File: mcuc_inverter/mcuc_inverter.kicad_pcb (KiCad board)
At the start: 4 copper layers, 200 x 132 mm, 465 parts, among them J1101 Coldplate NTC, J1201 CAN bus (H/L/GND/nc), J1202 GCT USB4085-GF-A, J1203 Aux 12-24 V in, J1204 Main contactor coil, J1205 Hall + motor temp, J1206 Encoder / SinCos, J1207 Resolver, J1208 FTSH-105-01-L-DV-K, J401 DC_INPUT_P tap - 6.3mm FASTON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, J402 to R401 chassis - 6.3mm FASTO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, J403 R401 return to DC_BUS_P tap -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, J404 from R424 chassis - 6.3mm FAS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, J405 DC_BUS_N tap - 6.3mm FASTON /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, J501 HOYS U harness - JST PA B05B-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, J502 HOYS V harness - JST PA B05B-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, J503 HOYS W harness - JST PA B05B-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, K401 HV DC precharge relay, >=450 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, Q311 BSS138 [TBV], Q321 BSS138 [TBV], Q331 BSS138 [TBV], Q341 BSS138 [TBV], Q351 BSS138 [TBV], Q361 BSS138 [TBV], Q401 AO3400-class [TBV], Q402 AO3400-class [TBV], Q403 C3M0350120J [TBV], Q601 CSD18543Q3A-class [TBV], Q602 CSD18543Q3A-class [TBV], Q603 CSD18543Q3A-class [TBV], Q604 CSD18543Q3A-class [TBV], Q605 CSD18543Q3A-class [TBV], T601 custom flyback per DER-948Q T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, T602 750316856, T603 750316856, T604 750316856, T605 750316856, U1 STM32F405VGT6, U1201 ISO1042DWR, U1202 USBLC6-2SC6, U201 FS02MR12A8MA2B, U301 1ED3491MC12M, U302 1ED3491MC12M, U303 1ED3491MC12M, U304 1ED3491MC12M, U305 1ED3491MC12M, U306 1ED3491MC12M, U401 VOM1271T, U504 TLV7032/LM2903-class open-dra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, U505 TLV7032/LM2903-class open-dra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, U506 TLV7032/LM2903-class open-dra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, U601 INN3990CQ, U603 LM5175RHFR, U604 LM74610QDGKRQ1, U605 LMR51430XDDCR, U606 LMR51430XDDCR, U607 TLV1117-33, U608 NXE2S0505MC, U609 SN6505BDBVR, U610 SN6505BDBVR, U611 SN6505BDBVR, U612 SN6505BDBVR, U701 AMC1311BDWV, U702 MCP1804T-3302I/OT, U703 TLV9061/OPA320-class [TBV], U801 AD2S1205, U802 AD8397, U803 APX809-46, U804 74LVC1G11, U901 SN74LVC00APWR, U902 SN74ALVC08PWR, U903 SN74ALVC08PWR, U904 SN74AUP1G74DCUR, Y1 8MHz, Y801 8.192MHz ABM3B [TBV]

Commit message: PCB placement complete: HV domains correct, 0 DRC violations
Resolves all 72 clearance violations that correct HV netclassification
exposed, plus the 37 from the earlier wave. The board now has 0
clearance, 0 courtyard, 0 hole and 0 parity violations with the full
HV rule set genuinely applied.

The substantive fix was structural, not cosmetic: the bus-sense
high-side block had been placed in low-voltage territory because no
pocket existed in the HV zone, and its barrier-crossing transformer
T701 - a reinforced part with 9.2 mm creepage, the element that
isolates the bus-voltage amplifier from the 450 V rail - was sitting
entirely inside LV. It now genuinely straddles: secondary pins inside
HV_DOMAIN, primary pins in LV, 11.31 mm row separation, with its own
BARRIER copper keepout on all four layers cloned from the existing
isolator barriers (17 barriers now).

The whole HV sub-block moved with it - rectifiers, reservoir and
bypass capacitors, the LDO, the divider tail - rather than being
scattered, and the LV sub-block (SN6505B driver, output stage) stayed
together below the transformer primary. No HV_DOMAIN area needed
extending; the existing polygon had room once the module's press-fit
mounting holes were routed around.

Nine of the 72 were unrelated: T601's DC_BUS_N pin against LV
decoupling. Those capacitors moved closer to the regulators they
serve as a side effect - C654 from 17 mm to 7 mm, C655 from 28 mm to
5 mm - which is better for the buck loops anyway.

One item left open honestly: C655's ground stitching via was deleted
rather than relocated, because there is no GND pour near U606 - the
module region is carved out of the plane - so the via could only
dangle. Its ground now depends on routing, like U606's other pins.

Co-Authored-By: Claude Fable 5 <noreply@anthropic.com>
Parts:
- added C1205: 4.7uF, Capacitor_SMD:C_0805_2012Metric, F.Cu at (182.4, 20.6)
- added C318: 1u 50V X7R, Capacitor_SMD:C_0805_2012Metric, F.Cu at (47.9, 105.9)
- added C319: 100n 50V X7R, Capacitor_SMD:C_0603_1608Metric, F.Cu at (42.6, 108.1)
- added C328: 1u 50V X7R, Capacitor_SMD:C_0805_2012Metric, F.Cu at (78.6, 97.9)
- added C329: 100n 50V X7R, Capacitor_SMD:C_0603_1608Metric, F.Cu at (83.1, 95.9)
- added C338: 1u 50V X7R, Capacitor_SMD:C_0805_2012Metric, F.Cu at (138.6, 106.6)
- added C339: 100n 50V X7R, Capacitor_SMD:C_0603_1608Metric, F.Cu at (142.1, 105.6)
- added C348: 1u 50V X7R, Capacitor_SMD:C_0805_2012Metric, F.Cu at (42.9, 52.4)
- added C349: 100n 50V X7R, Capacitor_SMD:C_0603_1608Metric, F.Cu at (47.4, 54.9)
- added C358: 1u 50V X7R, Capacitor_SMD:C_0805_2012Metric, F.Cu at (88.9, 55.4)
- added C359: 100n 50V X7R, Capacitor_SMD:C_0603_1608Metric, F.Cu at (86.6, 55.1)
- added C368: 1u 50V X7R, Capacitor_SMD:C_0805_2012Metric, F.Cu at (135.9, 55.4)
- added C369: 100n 50V X7R, Capacitor_SMD:C_0603_1608Metric, F.Cu at (133.6, 55.1)
- added C420: 100nF, Capacitor_SMD:C_0603_1608Metric, F.Cu at (64.4, 64.1)
- added C421: 1nF, Capacitor_SMD:C_0603_1608Metric, F.Cu at (25.6, 110.0)
- added C510: 1nF, Capacitor_SMD:C_0603_1608Metric, F.Cu at (169.9, 59.1)
- added C511: 100nF, Capacitor_SMD:C_0603_1608Metric, F.Cu at (169.9, 57.1)
- added C512: 1nF, Capacitor_SMD:C_0603_1608Metric, F.Cu at (168.6, 71.9)
- added C513: 100nF, Capacitor_SMD:C_0603_1608Metric, F.Cu at (169.9, 69.1)
- added C514: 1nF, Capacitor_SMD:C_0603_1608Metric, F.Cu at (169.9, 79.1)
- added C515: 100nF, Capacitor_SMD:C_0603_1608Metric, F.Cu at (169.9, 77.1)
- added C516: 1nF, Capacitor_SMD:C_0603_1608Metric, F.Cu at (169.9, 87.9)
- added C641: 220nF 50V X7R, Capacitor_SMD:C_0603_1608Metric, F.Cu at (104.1, 33.1)
- added C649: 220nF 50V X7R, Capacitor_SMD:C_0603_1608Metric, F.Cu at (100.0, 35.0)
- added C654: 1uF 16V X7R, Capacitor_SMD:C_0603_1608Metric, F.Cu at (94.5, 18.4)
- added C655: 1uF 16V X7R, Capacitor_SMD:C_0603_1608Metric, F.Cu at (108.0, 43.8)
- added C684: 10uF 25V X7R, Capacitor_SMD:C_0805_2012Metric, F.Cu at (42.6, 110.9)
- added C685: 10uF 25V X7R, Capacitor_SMD:C_0805_2012Metric, F.Cu at (108.1, 102.9)
- added C686: 10uF 25V X7R, Capacitor_SMD:C_0805_2012Metric, F.Cu at (144.1, 107.9)
- added C687: 10uF 25V X7R, Capacitor_SMD:C_0805_2012Metric, F.Cu at (131.9, 59.1)
- added C711: 10uF, Capacitor_SMD:C_0805_2012Metric, F.Cu at (25.5, 71.0)
- added C712: 100nF, Capacitor_SMD:C_0603_1608Metric, F.Cu at (25.5, 68.0)
- added C713: 10uF, Capacitor_SMD:C_0805_2012Metric, F.Cu at (27.2, 48.1)
- added C906: 100n, Capacitor_SMD:C_0603_1608Metric, F.Cu at (164.1, 24.1)
- added C907: 220n, Capacitor_SMD:C_0603_1608Metric, F.Cu at (165.1, 20.4)
- added D404: SMBJ24A, Diode_SMD:D_SMB, F.Cu at (33.7, 80.3)
- added D405: SMBJ24A, Diode_SMD:D_SMB, F.Cu at (8.16, 79.1)
- added D620: BZX384-C9V1 [TBV], Diode_SMD:D_SOD-323, F.Cu at (42.0, 42.6)
- added D621: MMSZ5245C-E3-08 15V 2%, Diode_SMD:D_SOD-123, F.Cu at (47.0, 109.1)
- added D622: MMSZ5245C-E3-08 15V 2%, Diode_SMD:D_SOD-123, F.Cu at (87.5, 96.8)
- added D623: MMSZ5245C-E3-08 15V 2%, Diode_SMD:D_SOD-123, F.Cu at (138.8, 110.6)
- added D624: MMSZ5245C-E3-08 15V 2%, Diode_SMD:D_SOD-123, F.Cu at (128.0, 59.6)
- added D625: 1N4148W-7-F, Diode_SMD:D_SOD-123, F.Cu at (51.1, 109.5)
- added D626: 1N4148W-7-F, Diode_SMD:D_SOD-123, F.Cu at (103.5, 103.6)
- added D627: 1N4148W-7-F, Diode_SMD:D_SOD-123, F.Cu at (144.0, 110.6)
- added D628: 1N4148W-7-F, Diode_SMD:D_SOD-123, F.Cu at (124.1, 59.5)
- added D629: SMCJ36CA, Diode_SMD:D_SMC, F.Cu at (82.0, 51.1)
- added D630: MMSZ5243BT1G 13V, Diode_SMD:D_SOD-123, F.Cu at (94.8, 14.3)
- added D701: SS310 [TBV], Diode_SMD:D_SMC, F.Cu at (33.5, 43.4)
- added D702: SS310 [TBV], Diode_SMD:D_SMC, F.Cu at (23.0, 43.4)
- added D904: BAT54WS, Diode_SMD:D_SOD-323, F.Cu at (162.1, 24.0)
- added J406: PHASE_U motor output stud - M6 ring lug [TBV], MountingHole:MountingHole_6.4mm_M6_Pad_Via, F.Cu at (148.6, 124.1)
- added J407: PHASE_V motor output stud - M6 ring lug [TBV], MountingHole:MountingHole_6.4mm_M6_Pad_Via, F.Cu at (167.1, 124.1)
- added J408: PHASE_W motor output stud - M6 ring lug [TBV], MountingHole:MountingHole_6.4mm_M6_Pad_Via, F.Cu at (178.6, 105.1)
- added JP1201: TERM_H, Jumper:SolderJumper-2_P1.3mm_Bridged_RoundedPad1.0x1.5mm, F.Cu at (182.7, 24.3)
- added JP1202: TERM_L, Jumper:SolderJumper-2_P1.3mm_Bridged_RoundedPad1.0x1.5mm, F.Cu at (167.4, 24.1)
- added Q404: BSS138, Package_TO_SOT_SMD:SOT-23, F.Cu at (21.6, 110.0)
- added Q606: BCP56-16T1G, Package_TO_SOT_SMD:SOT-223-3_TabPin2, F.Cu at (57.8, 107.3)
- added Q607: BCP56-16T1G, Package_TO_SOT_SMD:SOT-223-3_TabPin2, F.Cu at (115.6, 100.3)
- added Q608: BCP56-16T1G, Package_TO_SOT_SMD:SOT-223-3_TabPin2, F.Cu at (151.8, 107.3)
- added Q609: BCP56-16T1G, Package_TO_SOT_SMD:SOT-223-3_TabPin2, F.Cu at (118.3, 57.6)
- added Q610: DMP6023LE-13, Package_TO_SOT_SMD:SOT-223-3_TabPin2, F.Cu at (139.3, 64.3)
- added R317: 2.49k 1% (zener preload 6.0mA), Resistor_SMD:R_1206_3216Metric, F.Cu at (41.3, 104.7)
- added R327: 2.49k 1% (zener preload 6.0mA), Resistor_SMD:R_1206_3216Metric, F.Cu at (82.4, 98.3)
- added R337: 2.49k 1% (zener preload 6.0mA), Resistor_SMD:R_1206_3216Metric, F.Cu at (135.3, 104.7)
- added R347: 2.49k 1% (zener preload 6.0mA), Resistor_SMD:R_1206_3216Metric, F.Cu at (43.9, 55.0)
- added R428: 10k, Resistor_SMD:R_0603_1608Metric, F.Cu at (27.0, 107.2)
- added R429: 10k, Resistor_SMD:R_0603_1608Metric, F.Cu at (66.4, 64.1)
- added R513: 100R, Resistor_SMD:R_0603_1608Metric, F.Cu at (172.6, 58.4)
- added R514: 100k, Resistor_SMD:R_0603_1608Metric, F.Cu at (167.1, 58.4)
- added R515: 1M, Resistor_SMD:R_0603_1608Metric, F.Cu at (168.6, 61.9)
- added R517: 100R, Resistor_SMD:R_0603_1608Metric, F.Cu at (169.9, 67.1)
- added R518: 100k, Resistor_SMD:R_0603_1608Metric, F.Cu at (169.9, 65.1)
- added R519: 1M, Resistor_SMD:R_0603_1608Metric, F.Cu at (167.1, 68.4)
- added R521: 100R, Resistor_SMD:R_0603_1608Metric, F.Cu at (167.1, 79.9)
- added R522: 100k, Resistor_SMD:R_0603_1608Metric, F.Cu at (165.1, 79.9)
- added R523: 1M, Resistor_SMD:R_0603_1608Metric, F.Cu at (170.9, 84.9)
- added R612: 39k, Resistor_SMD:R_1206_3216Metric, F.Cu at (30.3, 4.20)
- added R613: 39k, Resistor_SMD:R_1206_3216Metric, F.Cu at (27.5, 4.45)
- added R614: 39k, Resistor_SMD:R_1206_3216Metric, F.Cu at (24.8, 4.45)
- added R615: 39k, Resistor_SMD:R_1206_3216Metric, F.Cu at (22.0, 4.45)
- added R616: 300k, Resistor_SMD:R_1206_3216Metric, F.Cu at (43.3, 3.69)
- added R617: 300k, Resistor_SMD:R_1206_3216Metric, F.Cu at (41.5, 29.0)
- added R618: 300k, Resistor_SMD:R_1206_3216Metric, F.Cu at (41.5, 34.0)
- added R619: 300k, Resistor_SMD:R_1206_3216Metric, F.Cu at (41.5, 39.0)
- added R630: 210k, Resistor_SMD:R_0603_1608Metric, F.Cu at (42.0, 45.3)
- added R644: 470R 1%, Resistor_SMD:R_0603_1608Metric, F.Cu at (39.6, 110.4)
- added R645: 470R 1%, Resistor_SMD:R_0603_1608Metric, F.Cu at (105.4, 95.9)
- added R646: 470R 1%, Resistor_SMD:R_0603_1608Metric, F.Cu at (134.4, 111.1)
- added R647: 470R 1%, Resistor_SMD:R_0603_1608Metric, F.Cu at (127.1, 57.1)
- added R648: 100k, Resistor_SMD:R_0603_1608Metric, F.Cu at (93.9, 9.89)
- added R840: 1.00k, Resistor_SMD:R_0603_1608Metric, F.Cu at (185.9, 23.1)
- added R841: 10.0k, Resistor_SMD:R_0603_1608Metric, F.Cu at (189.4, 23.1)
- added T701: 750313734, mcuc:WE_750313734, F.Cu at (20.3, 57.5)
- added U402: SN74LVC1G97DBVR, Package_TO_SOT_SMD:SOT-23-6, F.Cu at (36.4, 62.7)
- added U507: OPA376AIDBVR, Package_TO_SOT_SMD:SOT-23-5, F.Cu at (172.0, 62.1)
- added U508: OPA376AIDBVR, Package_TO_SOT_SMD:SOT-23-5, F.Cu at (172.0, 72.1)
- added U509: OPA376AIDBVR, Package_TO_SOT_SMD:SOT-23-5, F.Cu at (172.0, 82.1)
- added U704: SN6505BDBVR, Package_TO_SOT_SMD:SOT-23-6, F.Cu at (20.5, 67.5)
- C1, C1101, C1102, C12, C1201, C1202, C1203, C13, C14, C2, C3, C311, C312, C314, C316, C321, C322, C324, C326, C331, C332, C334, C336, C341, C342, C344, C346, C351, C352, C354, C356, C361, C362, C364, C366, C4, C5, C501, C502, C503, C504, C505, C506, C507, C508, C509, C6, C611, C613, C622, C623, C624, C625, C626, C627, C631, C642, C646, C652, C661, C663, C665, C667, C669, C671, C673, C675, C677, C679, C681, C683, C701, C702, C706, C707, C708, C709, C710, C8, C801, C802, C803, C804, C805, C806, C807, C808, C809, C810, C811, C812, C813, C814, C815, C817, C819, C820, C9, C901, C902, C903, C904, C905: footprint C_0603_1608Metric -> Capacitor_SMD:C_0603_1608Metric
- C10, C11, C1204, C313, C315, C323, C325, C333, C335, C343, C345, C353, C355, C363, C365, C620, C621, C650, C651, C653, C660, C662, C664, C666, C668, C670, C672, C674, C676, C678, C680, C682, C7: footprint C_0805_2012Metric -> Capacitor_SMD:C_0805_2012Metric
- C317, C327, C337, C347, C357, C367: value 100p [TBV] -> 22p 50V C0G - DNP; footprint C_0603_1608Metric -> Capacitor_SMD:C_0603_1608Metric
- C601, C602: value 0.68uF 630V film [TBV] -> 0.68uF 630VDC X2 film; footprint C_0603_1608Metric -> Capacitor_THT:C_Rect_L26.5mm_W10.5mm_P22.50mm_MKS4
- C603: value 10nF 1kV [TBV] -> 6.8nF 630V C0G; footprint C_0603_1608Metric -> Capacitor_SMD:C_1210_3225Metric
- C604: value 10uF 50V [TBV] -> 10uF 50V X7R; footprint C_0603_1608Metric -> Capacitor_SMD:C_1210_3225Metric
- C606: value 4.7uF 25V X7R [TBV] -> 0.47uF 50V X7R; footprint C_0603_1608Metric -> Capacitor_SMD:C_0805_2012Metric
- C607: value 100nF [TBV] -> 100nF 50V X7R; footprint C_0603_1608Metric -> Capacitor_SMD:C_0805_2012Metric
- C608: value 1nF 100V [TBV] -> 1nF 200V C0G; footprint C_0603_1608Metric -> Capacitor_SMD:C_0805_2012Metric
- C609, C610: footprint CP_Elec_8x10.5 -> Capacitor_SMD:CP_Elec_8x10.5
- C612: value 330pF [TBV] -> 270pF; footprint C_0603_1608Metric -> Capacitor_SMD:C_0603_1608Metric
- C614: footprint C_0603_1608Metric -> Capacitor_SMD:C_0805_2012Metric
- C628: value 100pF [TBV] -> 130pF; footprint C_0603_1608Metric -> Capacitor_SMD:C_0603_1608Metric
- C629, C630, C643, C644, C647, C648: footprint C_1210_3225Metric -> Capacitor_SMD:C_1210_3225Metric
- C640, C645: value 2.2uF 50V [TBV] -> 10uF 50V X7R; footprint C_0805_2012Metric -> Capacitor_SMD:C_1210_3225Metric
- C703: value 100nF -> 100pF; footprint C_0603_1608Metric -> Capacitor_SMD:C_0603_1608Metric
- C816, C818: value 100nF -> 1nF; footprint C_0603_1608Metric -> Capacitor_SMD:C_0603_1608Metric
- D1201, D801, D802, D803, D804, D805, D806, D807, D808, D809, D901, U803: footprint SOT-23 -> Package_TO_SOT_SMD:SOT-23
- D1202, D1203: footprint LED_0805_2012Metric -> LED_SMD:LED_0805_2012Metric
- D311, D321, D331, D341, D351, D361, D602: footprint D_SOD-323 -> Diode_SMD:D_SOD-323
- D312, D313, D322, D323, D332, D333, D342, D343, D352, D353, D362, D363, D601: footprint D_SMA -> Diode_SMD:D_SMA
- D401: value BAS316 [TBV] -> ES1G; footprint D_SOD-323 -> Diode_SMD:D_SMA
- D402: value BAS316 [TBV] -> ES2G; footprint D_SOD-323 -> Diode_SMD:D_SMB
- D403: value MM3Z18VT1G -> MMSZ5245BT1G; footprint D_SOD-323 -> Diode_SMD:D_SOD-123
- D603, D604, D605, D606, D608, D609, D611, D612, D614, D615: footprint D_SMC -> Diode_SMD:D_SMC
- D607, D610, D613, D616: value BZX384-C5V1 [TBV] -> MM3Z4V7ST1G 4.7V; footprint D_SOD-323 -> Diode_SMD:D_SOD-323
- D902: value OCP -> APT2012SURCK red (OCP); footprint LED_0805_2012Metric -> LED_SMD:LED_0805_2012Metric
- D903: value FAULT -> APT2012SYCK amber (DRV FLT); footprint LED_0805_2012Metric -> LED_SMD:LED_0805_2012Metric
- E801, FB1: footprint L_0805_2012Metric -> Inductor_SMD:L_0805_2012Metric
- J1101: footprint JST_PH_B2B-PH-K_1x02_P2.00mm_Vertical -> Connector_JST:JST_PH_B2B-PH-K_1x02_P2.00mm_Vertical
- J1201: footprint JST_PH_B4B-PH-K_1x04_P2.00mm_Vertical -> Connector_JST:JST_PH_B4B-PH-K_1x04_P2.00mm_Vertical
- J1202: footprint USB_C_Receptacle_GCT_USB4085 -> Connector_USB:USB_C_Receptacle_GCT_USB4085
- J1203: footprint JST_VH_B2P-VH_1x02_P3.96mm_Vertical -> Connector_JST:JST_VH_B2P-VH_1x02_P3.96mm_Vertical
- J1204: footprint JST_VH_B4P-VH_1x04_P3.96mm_Vertical -> Connector_JST:JST_VH_B4P-VH_1x04_P3.96mm_Vertical
- J1205, J1206: footprint JST_SH_SM08B-SRSS-TB_1x08-1MP_P1.00mm_Horizontal -> Connector_JST:JST_SH_SM08B-SRSS-TB_1x08-1MP_P1.00mm_Horizontal
- J1207: footprint JST_SH_SM06B-SRSS-TB_1x06-1MP_P1.00mm_Horizontal -> Connector_JST:JST_SH_SM06B-SRSS-TB_1x06-1MP_P1.00mm_Horizontal
- J1208: footprint PinHeader_2x05_P1.27mm_Vertical_SMD -> Connector_PinHeader_1.27mm:PinHeader_2x05_P1.27mm_Vertical_SMD
- J401, J402, J403, J404, J405: footprint MountingHole_4.3mm_M4_Pad_Via -> MountingHole:MountingHole_4.3mm_M4_Pad_Via
- J501, J502, J503: footprint JST_PH_B5B-PH-K_1x05_P2.00mm_Vertical -> mcuc:JST_PA_B05B-PASK-1_1x05_P2.00mm_Vertical
- K401: value HV DC precharge relay, >=450 V DC contacts [TBV] -> HFE80V-20C/450-12-HTPAJ; footprint HFE80V_HTPAJ -> mcuc:HFE80V_HTPAJ
- L601: footprint L_Bourns_SRP6060FA -> Inductor_SMD:L_Bourns_SRP6060FA
- L602: value SRP5030TA-4R7M 4.7uH 6A -> SRP6060FA-100M 10uH 7.6A; footprint L_Bourns_SRP5030T -> Inductor_SMD:L_Bourns_SRP6060FA
- L603: footprint L_Bourns_SRR1260 -> Inductor_SMD:L_Bourns_SRR1260
- Q311, Q321, Q331, Q341, Q351, Q361: value BSS138 [TBV] -> BSS316N; footprint SOT-23 -> Package_TO_SOT_SMD:SOT-23
- Q401: value AO3400-class [TBV] -> NVR5198NLT1G; footprint SOT-23 -> Package_TO_SOT_SMD:SOT-23
- Q402: value AO3400-class [TBV] -> DMN6068LK3-13; footprint SOT-23 -> Package_TO_SOT_SMD:TO-252-3_TabPin2
- Q403: footprint TO-263-7_TabPin8 -> Package_TO_SOT_SMD:TO-263-7_TabPin8
- Q601, Q602, Q603, Q604, Q605: footprint VSON-8_3.3x3.3mm_P0.65mm_NexFET -> Package_SON:VSON-8_3.3x3.3mm_P0.65mm_NexFET
- R1, R1101, R1102, R1103, R1104, R1202, R1203, R1204, R1205, R1206, R1207, R1208, R1209, R311, R321, R331, R341, R351, R361, R391, R392, R393, R402, R403, R404, R405, R425, R426, R501, R505, R509, R606, R607, R609, R610, R611, R620, R621, R624, R625, R626, R627, R705, R706, R707, R708, R801, R802, R803, R804, R805, R806, R807, R808, R809, R810, R811, R812, R813, R814, R815, R821, R822, R823, R824, R825, R826, R827, R828, R829, R830, R831, R832, R833, R836, R839, R901, R902, R903, R904, R905, R906, R907, R908, R909, R910, R913, R914, RT1101: footprint R_0603_1608Metric -> Resistor_SMD:R_0603_1608Metric
- R312, R322, R332, R342, R352, R362: value 4.87k [TBV] -> 28.0k 1% (ADJA: soft-off 699mA); footprint R_0603_1608Metric -> Resistor_SMD:R_0603_1608Metric
- R313, R323, R333, R343, R353, R363: value 1.33k [TBV] -> 0R link (ADJB=VCC1); footprint R_0603_1608Metric -> Resistor_SMD:R_0603_1608Metric
- R314, R324, R334, R344, R354, R364: value 12 [TBV] -> 12R 1% 0.75W CRCW1206-HP; footprint R_1206_3216Metric -> Resistor_SMD:R_1206_3216Metric
- R315, R325, R335, R345, R355, R365: value 3.3 [TBV] -> 3R3 1% 0.75W CRCW1206-HP; footprint R_1206_3216Metric -> Resistor_SMD:R_1206_3216Metric
- R316, R326, R336, R346, R356, R366, R701, R702, R703, R704: footprint R_1206_3216Metric -> Resistor_SMD:R_1206_3216Metric
- R411, R412, R413, R414: value 18.7k 3W [TBV] -> 14k 2W; footprint R_2512_6332Metric -> Resistor_SMD:R_2512_6332Metric
- R427: value 100R -> 220R; footprint R_0603_1608Metric -> Resistor_SMD:R_0603_1608Metric
- R502, R506, R510: value 9.53k -> 6.19k 0.1%; footprint R_0603_1608Metric -> Resistor_SMD:R_0603_1608Metric
- R503, R507, R511: value 13.7k -> 6.19k 0.1%; footprint R_0603_1608Metric -> Resistor_SMD:R_0603_1608Metric
- R504, R508, R512: value 9.53k -> 8.62k 0.1%; footprint R_0603_1608Metric -> Resistor_SMD:R_0603_1608Metric
- R603, R604: value 390k 0.5W [TBV] -> 39k; footprint R_0603_1608Metric -> Resistor_SMD:R_1206_3216Metric
- R605: value 4.7R 0.5W [TBV] -> 4.7R; footprint R_0603_1608Metric -> Resistor_SMD:R_1206_3216Metric
- R608: value 10R [TBV] -> 10R; footprint R_0603_1608Metric -> Resistor_SMD:R_1206_3216Metric
- R622: value 10mR 1% [TBV] -> 30mR 1%; footprint R_2512_6332Metric -> Resistor_SMD:R_2512_6332Metric
- R623: value 88.7k 1% -> 97.6k 1%; footprint R_0603_1608Metric -> Resistor_SMD:R_0603_1608Metric
- R640: value 71.5k 1% -> 100k 1%; footprint R_0603_1608Metric -> Resistor_SMD:R_0603_1608Metric
- R641: value 9.76k 1% -> 24.9k 1%; footprint R_0603_1608Metric -> Resistor_SMD:R_0603_1608Metric
- R642: value 115k 1% -> 100k 1%; footprint R_0603_1608Metric -> Resistor_SMD:R_0603_1608Metric
- R643: value 6.04k 1% -> 9.09k 1%; footprint R_0603_1608Metric -> Resistor_SMD:R_0603_1608Metric
- R709, R710: value 7.50k -> 15.0k; footprint R_0603_1608Metric -> Resistor_SMD:R_0603_1608Metric
- R816, R817, R818: value 0R -> 1k; footprint R_0603_1608Metric -> Resistor_SMD:R_0603_1608Metric
- R834, R837: value 100k -> 10k; footprint R_0603_1608Metric -> Resistor_SMD:R_0603_1608Metric
- R835, R838: value 270k -> 27k; footprint R_0603_1608Metric -> Resistor_SMD:R_0603_1608Metric
- R911, R912: value 100R -> 2.2k; footprint R_0603_1608Metric -> Resistor_SMD:R_0603_1608Metric
- T601: footprint T_FLYBACK_EQ30 -> mcuc:T_FLYBACK_EQ30
- T602, T603, T604, T605: footprint WE_PPTI_750316856 -> mcuc:WE_PPTI_750316856
- TP1101, TP1102, TP1103, TP1104, TP1105, TP1106: footprint TestPoint_Pad_D1.5mm -> TestPoint:TestPoint_Pad_D1.5mm
- U1: footprint LQFP-100_14x14mm_P0.5mm -> Package_QFP:LQFP-100_14x14mm_P0.5mm
- U1201: footprint SOIC-16W_7.5x10.3mm_P1.27mm -> Package_SO:SOIC-16W_7.5x10.3mm_P1.27mm
- U1202, U609, U610, U611, U612: footprint SOT-23-6 -> Package_TO_SOT_SMD:SOT-23-6
- U201: footprint FS02MR12A8MA2B_PressFIT -> mcuc:FS02MR12A8MA2B_PressFIT
- U301, U302, U303, U304, U305, U306: footprint PG-DSO-16-28 -> mcuc:PG-DSO-16-28
- U401: footprint SOP-4_3.8x4.1mm_P2.54mm -> Package_SO:SOP-4_3.8x4.1mm_P2.54mm
- U504, U505, U506: value TLV7032/LM2903-class open-drain [TBV] -> TLV7022DDFR; footprint SOIC-8_3.9x4.9mm_P1.27mm -> Package_TO_SOT_SMD:Texas_DDF0008A_SOT-8_1.6x2.9mm_P0.65mm
- U601: footprint InSOP-24D -> mcuc:InSOP-24D
- U603: footprint VQFN-28-1EP_4x5mm_P0.5mm_EP2.55x3.55mm -> Package_DFN_QFN:VQFN-28-1EP_4x5mm_P0.5mm_EP2.55x3.55mm
- U604: footprint VSSOP-8_3x3mm_P0.65mm -> Package_SO:VSSOP-8_3x3mm_P0.65mm
- U605, U606: value LMR51430XDDCR -> LMR33630ADDAR; footprint SOT-23-6 -> Package_SO:SOIC-8-1EP_3.9x4.9mm_P1.27mm_EP2.95x4.9mm_Mask2.71x3.4mm
- U607: footprint SOT-223-3_TabPin2 -> Package_TO_SOT_SMD:SOT-223-3_TabPin2
- U608: footprint Converter_DCDC_Murata_NXExSxxxxMC_SMD -> Converter_DCDC:Converter_DCDC_Murata_NXExSxxxxMC_SMD
- U701: footprint SOIC-8_7.5x5.85mm_P1.27mm -> Package_SO:SOIC-8_7.5x5.85mm_P1.27mm
- U702, U703: footprint SOT-23-5 -> Package_TO_SOT_SMD:SOT-23-5
- U801: footprint LQFP-44_10x10mm_P0.8mm -> Package_QFP:LQFP-44_10x10mm_P0.8mm
- U802: footprint SOIC-8-1EP_3.9x4.9mm_P1.27mm_EP2.29x3mm -> Package_SO:SOIC-8-1EP_3.9x4.9mm_P1.27mm_EP2.29x3mm
- U804: footprint SOT-363_SC-70-6 -> Package_TO_SOT_SMD:SOT-363_SC-70-6
- U901, U902, U903: footprint TSSOP-14_4.4x5mm_P0.65mm -> Package_SO:TSSOP-14_4.4x5mm_P0.65mm
- U904: footprint VSSOP-8_2.3x2mm_P0.5mm -> Package_SO:VSSOP-8_2.3x2mm_P0.5mm
- Y1: footprint Crystal_SMD_5032-2Pin_5.0x3.2mm -> Crystal:Crystal_SMD_5032-2Pin_5.0x3.2mm
- Y801: footprint Crystal_SMD_Abracon_ABM3B-4Pin_5.0x3.2mm -> Crystal:Crystal_SMD_Abracon_ABM3B-4Pin_5.0x3.2mm
- moved C602 112.2 mm to (90.9, 125.7)
- moved C601 104.2 mm to (90.9, 113.9)
- moved L602 63.5 mm to (83.5, 76.6), turned to 90 degrees
- moved R707 35.3 mm to (62.1, 61.4)
- moved R405 34.7 mm to (62.4, 64.1), turned to 90 degrees
- moved R403 33.4 mm to (1.90, 90.9), turned to 90 degrees
- moved R402 28.2 mm to (58.6, 61.9)
- moved D402 25.0 mm to (3.16, 79.1), turned to 90 degrees
- moved U606 22.4 mm to (117.1, 42.9), turned to 0 degrees
- moved R708 20.4 mm to (3.89, 61.9)
- moved C346 20.0 mm to (51.6, 61.4), turned to 0 degrees
- moved U605 19.1 mm to (100.1, 14.6), turned to 0 degrees
- moved D401 18.4 mm to (18.9, 79.5)
- moved R710 18.0 mm to (37.1, 78.1)
- moved R404 16.9 mm to (1.90, 63.1)
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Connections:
- net Net-(D403-K) renamed /Precharge and contactor/Q403_G
- C602 pad 2: /Auxiliary power/DC_BUS_N -> /Precharge and contactor/DC_BUS_N
- C603 pad 2: Net-(C603-Pad2) -> /Auxiliary power/CLAMP_NODE
- C604 pad 2: /Auxiliary power/DC_BUS_N -> /Precharge and contactor/DC_BUS_N
- C606 pad 2: /Auxiliary power/DC_BUS_N -> /Precharge and contactor/DC_BUS_N
- C607 pad 2: /Auxiliary power/DC_BUS_N -> /Precharge and contactor/DC_BUS_N
- C620 pad 1: /AUX_IN -> /Auxiliary power/AUX_IN_P
- C621 pad 1: /AUX_IN -> /Auxiliary power/AUX_IN_P
- C642 pad 1: Net-(U605-CB) -> Net-(U605-BOOT)
- C646 pad 1: Net-(U606-CB) -> Net-(U606-BOOT)
- C662 pad 1: /VGD_HS1_P -> /Auxiliary power/VGD_HS1_RAW
- C663 pad 1: /VGD_HS1_P -> /Auxiliary power/VGD_HS1_RAW
- C668 pad 1: /VGD_HS2_P -> /Auxiliary power/VGD_HS2_RAW
- C669 pad 1: /VGD_HS2_P -> /Auxiliary power/VGD_HS2_RAW
- C674 pad 1: /VGD_HS3_P -> /Auxiliary power/VGD_HS3_RAW
- C675 pad 1: /VGD_HS3_P -> /Auxiliary power/VGD_HS3_RAW
- C680 pad 1: /VGD_LS_P -> /Auxiliary power/VGD_LS_RAW
- C681 pad 1: /VGD_LS_P -> /Auxiliary power/VGD_LS_RAW
- C701 pad 1: /VGD_LS_P -> /Bus voltage sensing/5V5_HV_RAW
- C701 pad 2: /VGD_LS_COM -> /Precharge and contactor/DC_BUS_N
- C702 pad 1: unconnected-(C702-Pad1) -> /Bus voltage sensing/3V3_HV
- C702 pad 2: /VGD_LS_COM -> /Precharge and contactor/DC_BUS_N
- C703 pad 2: /Auxiliary power/DC_BUS_N -> /Precharge and contactor/DC_BUS_N
- C706 pad 2: /Auxiliary power/DC_BUS_N -> /Precharge and contactor/DC_BUS_N
- C707 pad 2: /Auxiliary power/DC_BUS_N -> /Precharge and contactor/DC_BUS_N
- D401 pad 1: +12V -> Net-(D401-K)
- D402 pad 1: +12V -> Net-(D402-K)
- D403 pad 2: /Auxiliary power/DC_BUS_N -> /Precharge and contactor/DC_BUS_N
- D605 pad 1: /VGD_HS1_P -> /Auxiliary power/VGD_HS1_RAW
- D606 pad 1: /VGD_HS1_P -> /Auxiliary power/VGD_HS1_RAW
- D608 pad 1: /VGD_HS2_P -> /Auxiliary power/VGD_HS2_RAW
- D609 pad 1: /VGD_HS2_P -> /Auxiliary power/VGD_HS2_RAW
- D611 pad 1: /VGD_HS3_P -> /Auxiliary power/VGD_HS3_RAW
- D612 pad 1: /VGD_HS3_P -> /Auxiliary power/VGD_HS3_RAW
- D614 pad 1: /VGD_LS_P -> /Auxiliary power/VGD_LS_RAW
- D615 pad 1: /VGD_LS_P -> /Auxiliary power/VGD_LS_RAW
- D903 pad 1: /Supervisor and interlocks/FAULT_BKIN -> /Supervisor and interlocks/DRV_FAULT_IN
- J405 pad 1: /Auxiliary power/DC_BUS_N -> /Precharge and contactor/DC_BUS_N
- J501 pad 4: /I_REF_1 -> /Phase current sensing/HOYS_U_REF
- J502 pad 4: /I_REF_2 -> /Phase current sensing/HOYS_V_REF
- J503 pad 4: /I_REF_3 -> /Phase current sensing/HOYS_W_REF
- Q403 pad 2: /Auxiliary power/DC_BUS_N -> /Precharge and contactor/DC_BUS_N
- Q403 pad 3: /Auxiliary power/DC_BUS_N -> /Precharge and contactor/DC_BUS_N
- Q403 pad 4: /Auxiliary power/DC_BUS_N -> /Precharge and contactor/DC_BUS_N
- Q403 pad 5: /Auxiliary power/DC_BUS_N -> /Precharge and contactor/DC_BUS_N
- Q403 pad 6: /Auxiliary power/DC_BUS_N -> /Precharge and contactor/DC_BUS_N
- Q403 pad 7: /Auxiliary power/DC_BUS_N -> /Precharge and contactor/DC_BUS_N
- Q601 pad 5: /AUX_IN -> /Auxiliary power/AUX_IN_P
- R1202 pad 1: /Communications/CANH -> Net-(JP1201-B)
- R1203 pad 2: /Communications/CANL -> Net-(JP1202-B)
- R313 pad 2: GND -> +3.3V
- R323 pad 2: GND -> +3.3V
- R333 pad 2: GND -> +3.3V
- R343 pad 2: GND -> +3.3V
- R353 pad 2: GND -> +3.3V
- R363 pad 2: GND -> +3.3V
- R391 pad 2: /Gate drive/DRV_FAULT_IN -> /Supervisor and interlocks/DRV_FAULT_IN
- R414 pad 2: /Auxiliary power/DC_BUS_N -> /Precharge and contactor/DC_BUS_N
- R426 pad 2: /Auxiliary power/DC_BUS_N -> /Precharge and contactor/DC_BUS_N
- R427 pad 1: /DISCHARGE_EN -> /Precharge and contactor/DISCHARGE_DRV
- R502 pad 1: +3.3V -> /Phase current sensing/I_TH_U_HI
- R502 pad 2: Net-(U504A-+) -> /Phase current sensing/I_TH_U_FB
- R503 pad 1: Net-(U504A-+) -> /Phase current sensing/I_TH_U_FB
- R506 pad 1: +3.3V -> /Phase current sensing/I_TH_V_HI
- R506 pad 2: Net-(U505A-+) -> /Phase current sensing/I_TH_V_FB
- R507 pad 1: Net-(U505A-+) -> /Phase current sensing/I_TH_V_FB
- R510 pad 1: +3.3V -> /Phase current sensing/I_TH_W_HI
- R510 pad 2: Net-(U506A-+) -> /Phase current sensing/I_TH_W_FB
- R511 pad 1: Net-(U506A-+) -> /Phase current sensing/I_TH_W_FB
- R603 pad 2: Net-(C603-Pad2) -> Net-(R603-Pad2)
- R604 pad 2: Net-(C603-Pad2) -> Net-(R603-Pad2)
- R605 pad 1: Net-(C603-Pad2) -> /Auxiliary power/CLAMP_NODE
- R620 pad 1: /AUX_IN -> /Auxiliary power/AUX_IN_P
- R705 pad 2: /Auxiliary power/DC_BUS_N -> /Precharge and contactor/DC_BUS_N
- R909 pad 2: /Gate drive/DRV_FAULT_IN -> /Supervisor and interlocks/DRV_FAULT_IN
- R910 pad 1: /Gate drive/DRV_FAULT_IN -> /Supervisor and interlocks/DRV_FAULT_IN
- T601 pad 5: /Auxiliary power/DC_BUS_N -> /Precharge and contactor/DC_BUS_N
- U301 pad 6: /Gate drive/DRV_FAULT_IN -> /Supervisor and interlocks/DRV_FAULT_IN
- U302 pad 6: /Gate drive/DRV_FAULT_IN -> /Supervisor and interlocks/DRV_FAULT_IN
- U303 pad 6: /Gate drive/DRV_FAULT_IN -> /Supervisor and interlocks/DRV_FAULT_IN
- U304 pad 6: /Gate drive/DRV_FAULT_IN -> /Supervisor and interlocks/DRV_FAULT_IN
- U305 pad 6: /Gate drive/DRV_FAULT_IN -> /Supervisor and interlocks/DRV_FAULT_IN
- U306 pad 6: /Gate drive/DRV_FAULT_IN -> /Supervisor and interlocks/DRV_FAULT_IN
- U401 pad 3: /Auxiliary power/DC_BUS_N -> /Precharge and contactor/DC_BUS_N
- U504 pad 3: Net-(U504A-+) -> /Phase current sensing/I_TH_U_HI
- U505 pad 3: Net-(U505A-+) -> /Phase current sensing/I_TH_V_HI
- U506 pad 3: Net-(U506A-+) -> /Phase current sensing/I_TH_W_HI
- U601 pad 13: /Auxiliary power/DC_BUS_N -> /Auxiliary power/V_SENSE
- U601 pad 16: /Auxiliary power/DC_BUS_N -> /Precharge and contactor/DC_BUS_N
- U601 pad 17: /Auxiliary power/DC_BUS_N -> /Precharge and contactor/DC_BUS_N
- U601 pad 18: /Auxiliary power/DC_BUS_N -> /Precharge and contactor/DC_BUS_N
- U601 pad 19: /Auxiliary power/DC_BUS_N -> /Precharge and contactor/DC_BUS_N
- U603 pad 27: /AUX_IN -> /Auxiliary power/AUX_IN_P
- U603 pad 28: /AUX_IN -> /Auxiliary power/AUX_IN_P
- U605 pad 2: Net-(U605-SW) -> /Auxiliary power/AUX_15V
- U605 pad 4: /Auxiliary power/FB_5V -> unconnected-(U605-PG-Pad4)
- U605 pad 5: /Auxiliary power/AUX_15V -> /Auxiliary power/FB_5V
- U605 pad 6: Net-(U605-CB) -> Net-(U605-VCC)
- U606 pad 2: Net-(U606-SW) -> /Auxiliary power/AUX_15V
- U606 pad 4: /Auxiliary power/FB_12V -> unconnected-(U606-PG-Pad4)
- U606 pad 5: /Auxiliary power/AUX_15V -> /Auxiliary power/FB_12V
- U606 pad 6: Net-(U606-CB) -> Net-(U606-VCC)
- U701 pad 3: /Auxiliary power/DC_BUS_N -> /Precharge and contactor/DC_BUS_N
- U701 pad 4: /Auxiliary power/DC_BUS_N -> /Precharge and contactor/DC_BUS_N
- U702 pad 1: /VGD_LS_P -> /Bus voltage sensing/5V5_HV_RAW
- U702 pad 2: /VGD_LS_COM -> /Precharge and contactor/DC_BUS_N
- U702 pad 4: /VGD_LS_P -> /Bus voltage sensing/5V5_HV_RAW
- U903 pad 10: /Supervisor and interlocks/FAULT_BKIN -> GND
- U903 pad 12: Net-(U903-Pad12) -> /DRV_RST_IN
- U903 pad 8: Net-(U903-Pad12) -> unconnected-(U903-Pad8)
- U903 pad 9: /DRV_RST_IN -> GND
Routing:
- net GND: track 0.00 -> 139.8 mm, vias 0 -> 156
- net +3.3V: track 0.00 -> 24.3 mm, vias 0 -> 26
- net +5V: track 0.00 -> 8.13 mm, vias 0 -> 9
- net /CAN_GND: track 0.00 -> 6.00 mm, vias 0 -> 8
- net /Auxiliary power/AUX_15V: track 0.00 -> 2.25 mm, vias 0 -> 1
- added copper zone on F.Cu, net /Auxiliary power/VGD_LS_RAW

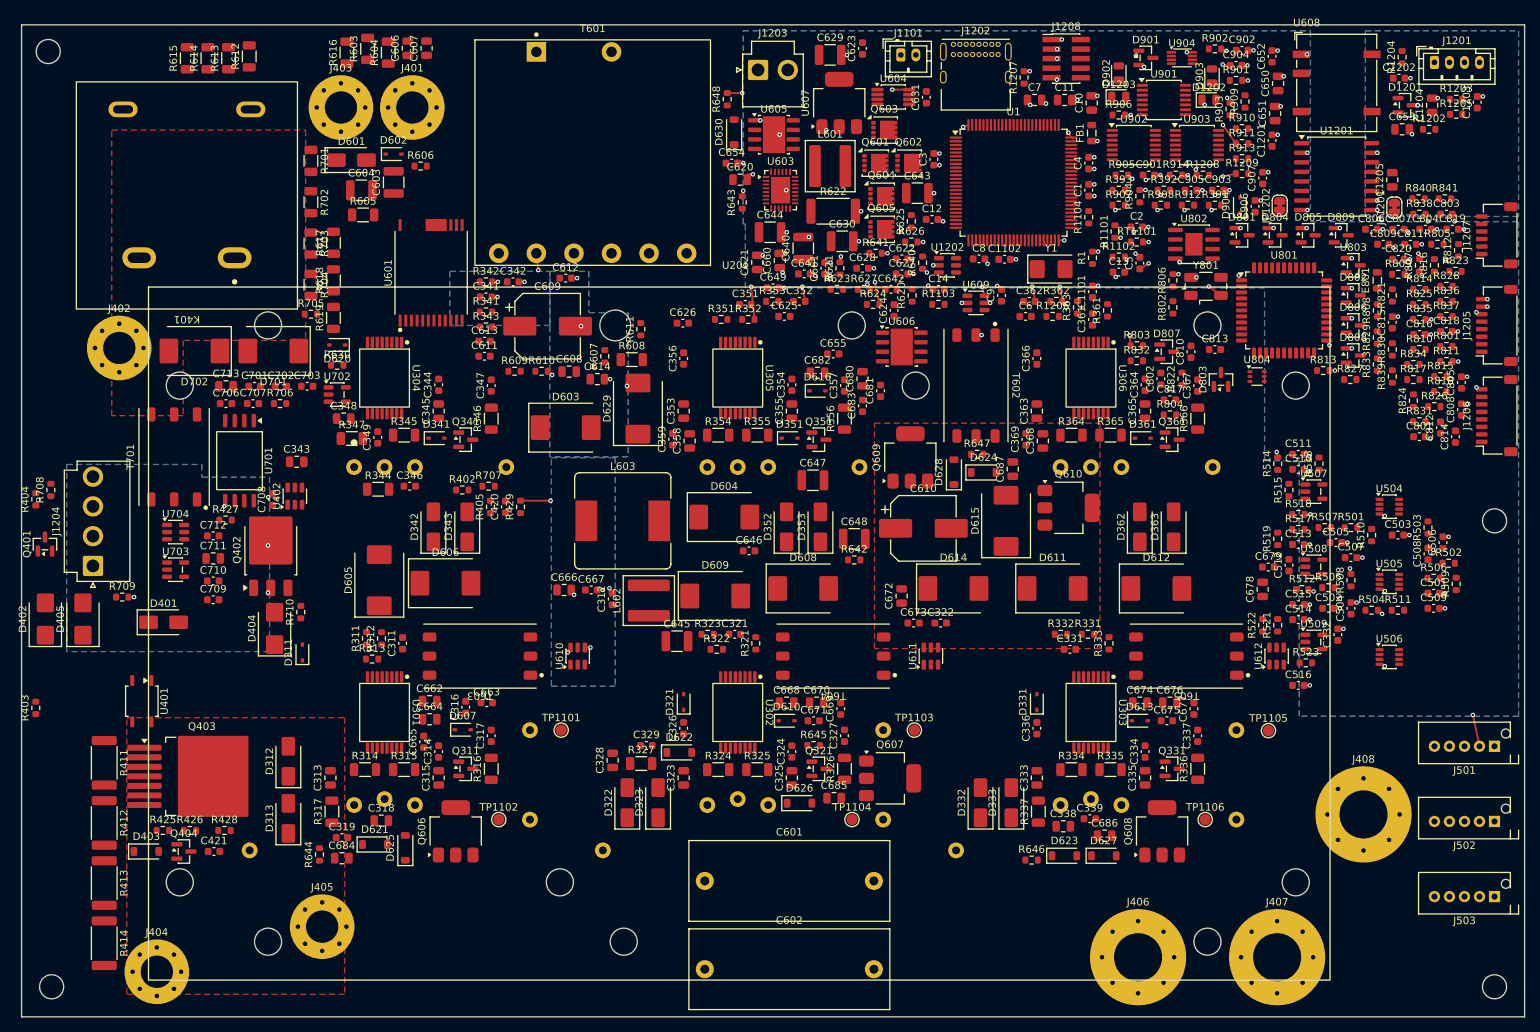
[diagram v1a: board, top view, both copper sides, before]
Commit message: Route critical loops; define the netclasses that were never defined
ROUTING: 1065 -> 553 unconnected (the "499" figure I had been
reporting was a kicad-cli display cap; the true count from the
connectivity API was 1065). 4031 tracks, 638 vias. Gate loops routed
on F.Cu without vias, driver supplies, aux power hot loops and much of
the signal set.

THIRD INSTANCE OF THE SAME DEFECT CLASS, and the worst yet: HV_BUS and
GATE were referenced by netclass_patterns but were NEVER DEFINED in
net_settings.classes - only Default existed. So the 2.0 mm HV
clearance and 3.0 mm HV track width this design has claimed throughout
were not being enforced by DRC at all. Only the custom HV_to_LV 6.4 mm
rule in the .kicad_dru was doing any work. Defining them immediately
surfaced 57 violations.

Of those: 52 were the GATE class flagging the gate driver's own
adjacent pins - a 0.65 mm-pitch package leaves ~0.25 mm between pads,
so a 0.25 mm clearance rule is tighter than the part it applies to.
GATE clearance corrected to 0.2 mm; it existed for track width, not
clearance.

44 REMAIN AND ARE REAL: parts in the flyback/RCD-clamp/divider block
are spaced for the 0.2 mm default while carrying near-full bus
voltage between them (e.g. the controller's bypass net against
DC_BUS_P). They need 2.0 mm. This is committed with the violations
VISIBLE rather than reverting the netclass definitions, because a
board that reports its real spacing problems is strictly better than
one whose rules silently never applied.

The routing agent's own judgement is worth recording: it deliberately
left the HV block mostly unrouted (13 of 87 connections) after an
earlier attempt "succeeded" by silently falling back to 0.25 mm track
at 0.2 mm clearance, producing 174 errors including DC_BUS_N-to-GND
violations of the 6.4 mm barrier. It ripped that out and disabled
width fallback for HV nets. An open net is always preferable to a
clearance violation.

Co-Authored-By: Claude Fable 5 <noreply@anthropic.com>
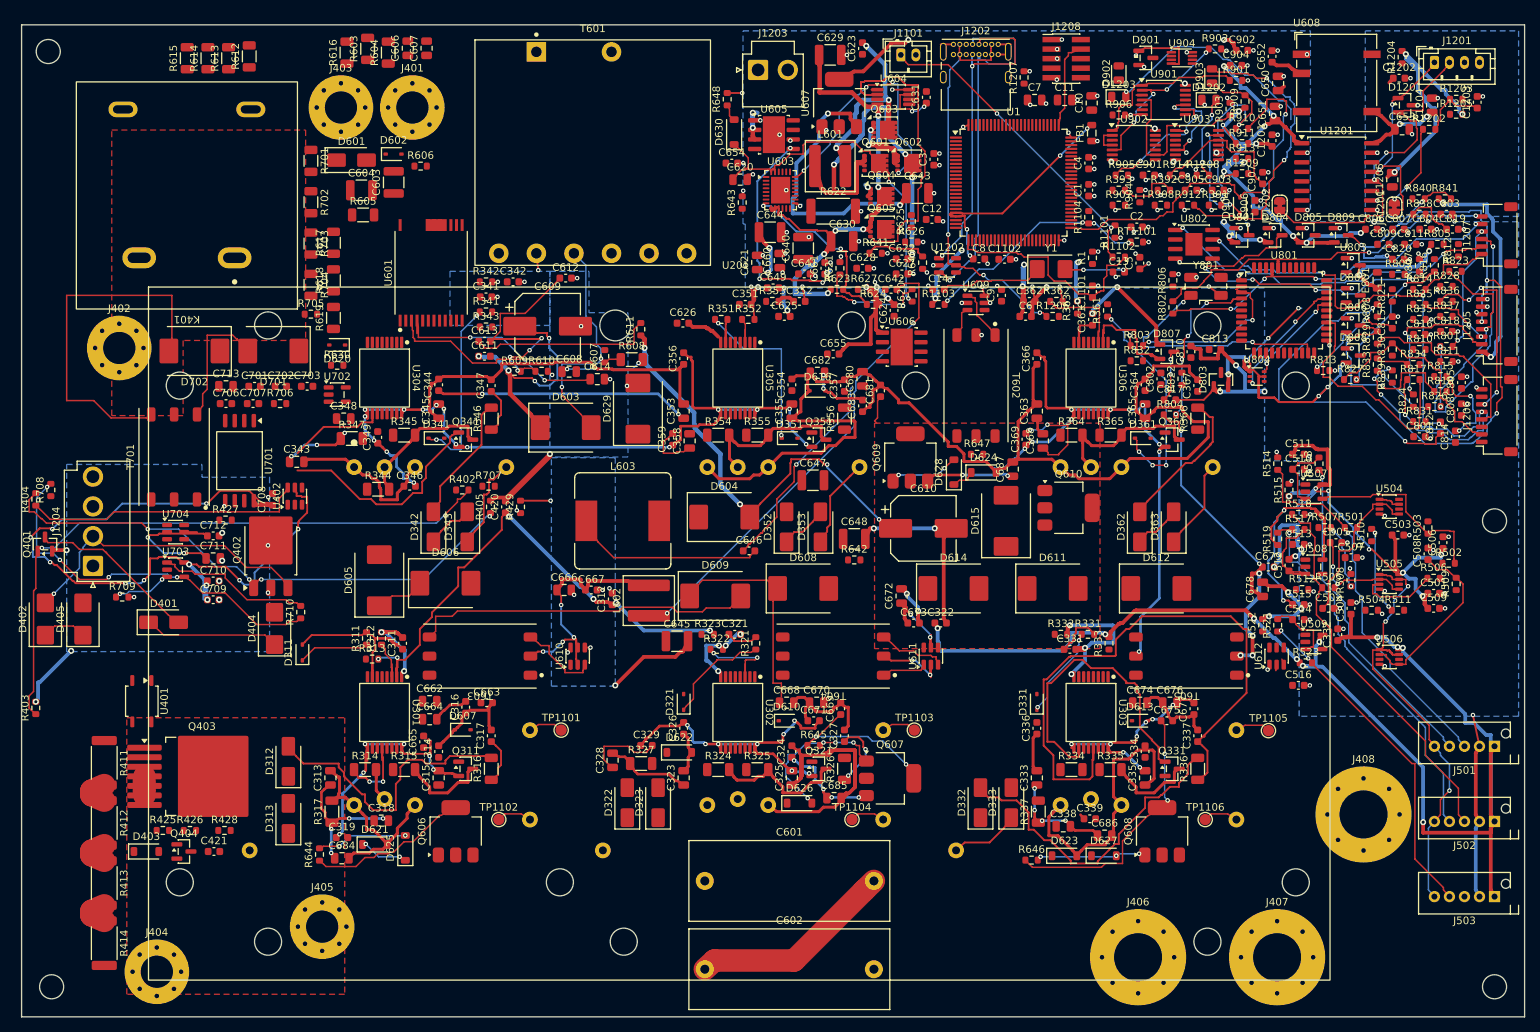
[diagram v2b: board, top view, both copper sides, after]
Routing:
- net +3.3V: track 24.3 -> 722.1 mm, vias 26 -> 93
- net GND: track 139.8 -> 430.0 mm, vias 156 -> 201
- net /VGD_LS_COM: track 0.00 -> 224.3 mm
- net +5V: track 8.13 -> 197.1 mm, vias 9 -> 30
- net /VGD_LS_N: track 0.00 -> 178.8 mm, vias 0 -> 28
- net /MOTOR_TEMP: track 0.00 -> 118.5 mm, vias 0 -> 9
- net /Auxiliary power/FLY_15V: track 0.00 -> 84.8 mm, vias 0 -> 8
- net Net-(Q401-G): track 0.00 -> 83.6 mm, vias 0 -> 2
- net Net-(U303-DESAT): track 0.00 -> 81.1 mm
- net /VGD_HS2_COM: track 0.00 -> 77.2 mm
- net Net-(Q402-G): track 0.00 -> 71.4 mm, vias 0 -> 4
- net /ENC_A: track 0.00 -> 65.6 mm, vias 0 -> 6
- net /Communications/RES_EXC_P: track 0.00 -> 65.0 mm, vias 0 -> 4
- net /Phase current sensing/OC_TRIP: track 0.00 -> 63.2 mm, vias 0 -> 3
- net Net-(U605-SW): track 0.00 -> 61.0 mm, vias 0 -> 2
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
